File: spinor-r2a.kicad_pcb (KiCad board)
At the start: 2 copper layers, 135 parts, among them Q1 NMOS, Q2 NMOS, Q3 NMOS, Q4 NMOS, Q5 NMOS, Q6 NMOS, U1 TCAN334G, U2 STM32G474CETx, U3 AS5047D, U4 DRV8353FSRTAR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

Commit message: start layout
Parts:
- removed C37: 100uF/63V, hn_lib:hn_C_Kemet_A768MS
- J1, J2, U3: moved to B.Cu
- J9: footprint hn_lib:hn_AMASS_XT30PW-F -> hn_lib:hn_AMASS_XT30PW-M
- L1: value 47uH/400mA -> FB/120R@100MHz; footprint hn_lib:hn_L_Bourns_SRN4026 -> hn_lib:hn_R_0805
- L3: value FB/120R@100MHz -> 47uH/400mA; footprint hn_lib:hn_R_0805 -> hn_lib:hn_L_Bourns_SRN4026
- moved H1 99.5 mm to (191.0, 58.5)
- moved L3 98.1 mm to (64.9, 28.6)
- moved L2 91.4 mm to (64.0, 58.0)
- moved H3 89.4 mm to (191.0, 100.5)
- moved D6 86.1 mm to (210.9, 63.8)
- moved C24 86.1 mm to (215.5, 59.3)
- moved C25 86.1 mm to (215.5, 62.7)
- moved C26 86.1 mm to (202.0, 68.5)
- moved C27 86.1 mm to (217.0, 66.0)
- moved D4 86.1 mm to (210.9, 58.9)
- moved D5 86.1 mm to (210.9, 61.3)
- moved R21 86.1 mm to (205.5, 68.2)
- moved R22 86.1 mm to (205.5, 70.2)
- moved C30 83.7 mm to (202.5, 93.8)
- moved R24 83.7 mm to (206.0, 93.5)
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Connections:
- net Net-(D10-A) renamed /FET_Half_Bridge_C/GATE_H_RAW
- net Net-(D11-A) renamed /FET_Half_Bridge_C/GATE_L_RAW
- net Net-(D4-A) renamed /FET_Half_Bridge_A/GATE_H_RAW
- net Net-(D5-A) renamed /FET_Half_Bridge_A/GATE_L_RAW
- net Net-(D7-A) renamed /FET_Half_Bridge_B/GATE_H_RAW
- net Net-(D8-A) renamed /FET_Half_Bridge_B/GATE_L_RAW
- L1 pad 1: /Power_Supply/3V3_BUCK_SW -> VDD
- L1 pad 2: VDD -> VDDA
- L2 pad 1: VDD -> VBUS
- L2 pad 2: VDDA -> Net-(U5-EN)
- L3 pad 1: VBUS -> /Power_Supply/3V3_BUCK_SW
- L3 pad 2: Net-(U5-EN) -> VDD
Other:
- board outline added: 50 x 63.5 mm

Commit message: placed more components
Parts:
- removed the C30 at (202.5, 93.8)
- removed the C31 at (205.7, 89.0)
- added C36: 4.7uF/50V, hn_lib:hn_C_1206, F.Cu at (81.2, 97.2)
- added C37: 100nF/50V, hn_lib:hn_C_0603, F.Cu at (74.2, 107.6)
- added C38: 4.7uF/50V, hn_lib:hn_C_1206, F.Cu at (132.8, 105.5)
- added C47: 4.7uF/50V, hn_lib:hn_C_1206, F.Cu at (127.8, 105.5)
- added C48: 4.7uF/50V, hn_lib:hn_C_1206, F.Cu at (125.2, 105.5)
- added C49: 4.7uF/50V, hn_lib:hn_C_1206, F.Cu at (126.2, 112.0)
- added C50: 1uF/6.3V, hn_lib:hn_C_0402, F.Cu at (89.3, 101.1)
- added C51: 1uF/6.3V, hn_lib:hn_C_0402, F.Cu at (89.3, 103.0)
- added C52: 4.7uF/50V, hn_lib:hn_C_1206, F.Cu at (169.5, 108.8)
- added C53: 4.7uF/50V, hn_lib:hn_C_1206, F.Cu at (169.5, 113.8)
- added C54: 4.7uF/50V, hn_lib:hn_C_1206, F.Cu at (127.8, 100.5)
- added C55: 4.7uF/50V, hn_lib:hn_C_1206, F.Cu at (125.2, 100.5)
- C24, C28, C33: value 4.7uF/50V -> 100nF/50V; footprint hn_lib:hn_C_1206 -> hn_lib:hn_C_0603
- C25, C29, C32: value 4.7uF/50V -> 2.2nF/6.3V; footprint hn_lib:hn_C_1206 -> hn_lib:hn_C_0402
- C34: value 100nF/50V -> 10uF/6.3V; footprint hn_lib:hn_C_0603 -> hn_lib:hn_C_0805
- C35: value 2.2nF/6.3V -> 100nF/50V; footprint hn_lib:hn_C_0402 -> hn_lib:hn_C_0603
- C39: value 2.2nF/6.3V -> 4.7uF/50V; footprint hn_lib:hn_C_0402 -> hn_lib:hn_C_1206
- C40, C42, C44: value 100nF/50V -> 4.7uF/50V; footprint hn_lib:hn_C_0603 -> hn_lib:hn_C_1206
- C41: value 10uF/6.3V -> 4.7uF/50V; footprint hn_lib:hn_C_0805 -> hn_lib:hn_C_1206
- C45, C46: value 1uF/6.3V -> 4.7uF/50V; footprint hn_lib:hn_C_0402 -> hn_lib:hn_C_1206
- D1, D2, D3: moved to B.Cu
- moved C35 158.4 mm to (74.2, 105.1)
- moved C33 157.0 mm to (74.2, 102.6)
- moved C32 151.4 mm to (79.8, 99.8)
- moved C34 139.2 mm to (78.5, 107.4)
- moved C41 113.1 mm to (157.0, 105.2), turned to 90 degrees
- moved C40 110.4 mm to (159.5, 105.2), turned to 90 degrees
- moved C39 107.2 mm to (153.0, 105.2), turned to 90 degrees
- moved D1 105.5 mm to (148.5, 129.0), turned to -90 degrees
- moved C43 102.0 mm to (126.2, 114.5), turned to 180 degrees
- moved C42 101.3 mm to (150.5, 105.2), turned to 90 degrees
- moved Y1 95.4 mm to (164.5, 85.2), turned to 180 degrees
- moved D2 95.1 mm to (147.6, 136.0), turned to -90 degrees
- moved U1 94.4 mm to (170.2, 95.2), turned to -90 degrees
- moved D3 93.4 mm to (149.4, 136.0), turned to -90 degrees
- moved C24 91.6 mm to (136.8, 106.0), turned to -90 degrees
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- renumbered C36 to C30, C38 to C31
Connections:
- C16 pad 1: GND -> GNDPWR
- C17 pad 1: GND -> GNDPWR
- C17 pad 2: GND -> GNDPWR
- C19 pad 2: GND -> GNDPWR
- C24 pad 2: GND -> /FET_Half_Bridge_A/SHUNT_P
- C25 pad 1: VBUS -> /FET_Half_Bridge_A/SHUNT_P
- C25 pad 2: GND -> GNDPWR
- C26 pad 2: /FET_Half_Bridge_A/SHUNT_P -> /FET_Half_Bridge_B/SHUNT_P
- C27 pad 1: /FET_Half_Bridge_A/SHUNT_P -> /FET_Half_Bridge_B/SHUNT_P
- C27 pad 2: GND -> GNDPWR
- C28 pad 2: GND -> /FET_Half_Bridge_C/SHUNT_P
- C29 pad 1: VBUS -> /FET_Half_Bridge_C/SHUNT_P
- C29 pad 2: GND -> GNDPWR
- C30 pad 2: GND -> GNDPWR
- C31 pad 2: GND -> GNDPWR
- C32 pad 1: VBUS -> /Microcontroller/ADC1_IN3
- C33 pad 1: VBUS -> /Power_Supply/3V3_BUCK_SW
- C33 pad 2: GND -> Net-(U5-CB)
- C34 pad 1: VBUS -> VDD
- C34 pad 2: /FET_Half_Bridge_C/SHUNT_P -> GND
- C35 pad 1: /FET_Half_Bridge_C/SHUNT_P -> VBUS
- C39 pad 1: /Microcontroller/ADC1_IN3 -> VBUS
- C39 pad 2: GND -> GNDPWR
- C40 pad 1: /Power_Supply/3V3_BUCK_SW -> VBUS
- C40 pad 2: Net-(U5-CB) -> GNDPWR
- C41 pad 1: VDD -> VBUS
- C41 pad 2: GND -> GNDPWR
- C42 pad 2: GND -> GNDPWR
- C43 pad 1: Net-(U5-EN) -> VBUS
- C43 pad 2: GND -> GNDPWR
- C44 pad 1: Net-(U5-EN) -> VBUS
- C44 pad 2: GND -> GNDPWR
- C45 pad 1: /Microcontroller/ADC12_IN1 -> VBUS
- C45 pad 2: GND -> GNDPWR
- C46 pad 1: /Microcontroller/ADC12_IN2 -> VBUS
- C46 pad 2: GND -> GNDPWR
- D12 pad 2: GND -> GNDPWR
- D13 pad 2: GND -> GNDPWR
- D6 pad 2: GND -> GNDPWR
- D9 pad 2: GND -> GNDPWR
- J8 pad 1: GND -> GNDPWR
- J9 pad 1: GND -> GNDPWR
- R23 pad 2: GND -> GNDPWR
- R26 pad 2: GND -> GNDPWR
- R29 pad 2: GND -> GNDPWR
- U4 pad 10: GND -> GNDPWR
- U4 pad 11: GND -> GNDPWR
- U4 pad 20: GND -> GNDPWR
- U4 pad 38: GND -> GNDPWR
- U4 pad 39: /Integrated_FET_Driver/GND -> GND
- U4 pad 41: GND -> GNDPWR

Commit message: layout driver and 3v3 buck
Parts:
- removed C35: 100nF/50V, hn_lib:hn_C_0603
- removed L2: FB/120R@100MHz, hn_lib:hn_R_0805
- moved C37 58.0 mm to (129.8, 90.8), turned to -90 degrees
- moved L3 55.9 mm to (129.8, 85.5), turned to 90 degrees
- moved C33 53.7 mm to (125.8, 87.2), turned to 180 degrees
- moved C34 52.9 mm to (126.2, 84.8), turned to -90 degrees
- moved U5 49.5 mm to (126.5, 90.0)
- moved C36 45.4 mm to (126.5, 93.2), turned to 180 degrees
- moved C18 36.3 mm to (139.0, 86.0)
- moved C15 34.0 mm to (137.0, 96.0), turned to 90 degrees
- moved C20 34.0 mm to (134.0, 94.5), turned to -90 degrees
- moved C17 33.3 mm to (133.0, 91.0), turned to 180 degrees
- moved C19 29.9 mm to (135.5, 96.0), turned to -90 degrees
- moved C16 26.8 mm to (132.5, 92.5)
- moved C32 18.1 mm to (97.6, 96.5)
- moved R31 16.3 mm to (97.8, 100.5)
- moved R30 16.3 mm to (97.8, 98.5)
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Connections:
- net Net-(U5-CB) renamed /Power_Supply/3V3_BUCK_CP
- C17 pad 1: GNDPWR -> /Integrated_FET_Driver/DVDD
- C36 pad 1: Net-(U5-EN) -> VBUS
- C37 pad 1: Net-(U5-EN) -> VBUS
- U4 pad 38: GNDPWR -> /Integrated_FET_Driver/DVDD
- U4 pad 39: GND -> GNDPWR
- U5 pad 4: Net-(U5-EN) -> VBUS
- U5 pad 5: Net-(U5-EN) -> VBUS

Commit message: ok
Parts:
- removed C13, C4: 100nF/6.3V, hn_lib:hn_C_0402
- moved C1 96.7 mm to (170.2, 90.8)
- moved R1 93.9 mm to (166.2, 90.8), turned to 180 degrees
- moved R2 93.9 mm to (166.2, 92.6)
- moved C2 89.4 mm to (163.0, 84.8)
- moved C9 81.2 mm to (157.8, 93.5), turned to 180 degrees
- moved R9 79.3 mm to (154.2, 94.8), turned to 90 degrees
- moved R10 77.9 mm to (153.2, 94.8), turned to 90 degrees
- moved C50 77.3 mm to (164.2, 82.0)
- moved R11 76.6 mm to (152.2, 94.8), turned to 90 degrees
- moved J10 76.3 mm to (163.8, 77.8), turned to 180 degrees
- moved C51 75.9 mm to (162.2, 82.0)
- moved R12 75.3 mm to (151.2, 94.8), turned to 90 degrees
- moved C12 75.3 mm to (154.0, 80.2)
- moved C11 74.9 mm to (154.0, 81.2)
- moved R34 73.6 mm to (164.2, 80.0), turned to 180 degrees
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
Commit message: done routing!
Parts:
- removed J3, J4: ~, Connector_PinHeader_1.27mm:PinHeader_1x04_P1.27mm_Vertical
- removed R18: 4.7k, hn_lib:hn_R_0402
- removed R7, R8: 100R, hn_lib:hn_R_0402
- added C4: 100uF/63V, hn_lib:hn_C_Kemet_A768MS, F.Cu at (157.0, 131.0)
- added C58: 4.7uF/50V, hn_lib:hn_C_1206, B.Cu at (160.8, 105.5)
- added C59: 4.7uF/50V, hn_lib:hn_C_1206, B.Cu at (158.2, 105.5)
- added C60: 4.7uF/50V, hn_lib:hn_C_1206, B.Cu at (153.2, 105.5)
- added C61: 4.7uF/50V, hn_lib:hn_C_1206, B.Cu at (145.8, 105.5)
- added C62: 4.7uF/50V, hn_lib:hn_C_1206, B.Cu at (140.8, 105.5)
- added C63: 4.7uF/50V, hn_lib:hn_C_1206, B.Cu at (163.2, 105.5)
- added C64: 4.7uF/50V, hn_lib:hn_C_1206, B.Cu at (148.2, 105.5)
- added C65: 4.7uF/50V, hn_lib:hn_C_1206, B.Cu at (155.8, 105.5)
- added C66: 4.7uF/50V, hn_lib:hn_C_1206, B.Cu at (150.8, 105.5)
- added C67: 4.7uF/50V, hn_lib:hn_C_1206, B.Cu at (143.2, 105.5)
- added C68: 4.7uF/50V, hn_lib:hn_C_1206, B.Cu at (138.2, 105.5)
- added C69: 4.7uF/50V, hn_lib:hn_C_1206, B.Cu at (135.8, 105.5)
- added TP13: ~, Connector_PinHeader_1.00mm:PinHeader_1x01_P1.00mm_Vertical, F.Cu at (162.7, 92.3)
- D1: moved to F.Cu
- D13: moved to B.Cu
- J9: value ~ -> Conn_01x05; footprint hn_lib:hn_AMASS_XT30PW-M -> Connector_PinHeader_2.54mm:PinHeader_1x05_P2.54mm_Vertical
- moved J9 51.2 mm to (132.9, 76.2), turned to 90 degrees
- moved R14 22.5 mm to (170.9, 83.5), turned to 0 degrees
- moved R15 22.5 mm to (170.9, 84.5), turned to 0 degrees
- moved D13 15.7 mm to (132.8, 125.6)
- moved C3 5.59 mm to (148.5, 101.0), turned to 0 degrees
- moved R6 5.43 mm to (138.0, 79.4), turned to 90 degrees
- moved R3 4.94 mm to (141.0, 79.4), turned to 90 degrees
- moved R5 4.88 mm to (139.0, 79.4), turned to 90 degrees
- moved R4 4.70 mm to (140.0, 79.4), turned to 90 degrees
- moved R30 4.16 mm to (164.0, 80.5)
- moved R31 4.16 mm to (164.0, 81.5)
- moved C37 3.93 mm to (126.4, 92.8), turned to 180 degrees
- moved R1 3.34 mm to (165.2, 94.0)
- moved R10 3.26 mm to (156.5, 94.5)
- moved R11 3.26 mm to (155.5, 94.5)
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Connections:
- net /Microcontroller/CANH renamed /Microcontroller/CAN_P
- net /Microcontroller/CANL renamed /Microcontroller/CAN_N
- C16 pad 1: GNDPWR -> GND
- C17 pad 2: GNDPWR -> GND
- C18 pad 1: VDDA -> VDD
- C19 pad 2: GNDPWR -> GND
- C25 pad 2: GNDPWR -> GND
- C27 pad 2: GNDPWR -> GND
- C29 pad 2: GNDPWR -> GND
- C30 pad 2: GNDPWR -> GND
- C31 pad 2: GNDPWR -> GND
- C38 pad 2: GNDPWR -> GND
- C39 pad 2: GNDPWR -> GND
- C40 pad 2: GNDPWR -> GND
- C41 pad 2: GNDPWR -> GND
- C42 pad 2: GNDPWR -> GND
- C43 pad 2: GNDPWR -> GND
- C44 pad 2: GNDPWR -> GND
- C45 pad 2: GNDPWR -> GND
- C46 pad 2: GNDPWR -> GND
- C47 pad 2: GNDPWR -> GND
- C48 pad 2: GNDPWR -> GND
- C49 pad 2: GNDPWR -> GND
- C52 pad 2: GNDPWR -> GND
- C53 pad 2: GNDPWR -> GND
- C54 pad 2: GNDPWR -> GND
- C55 pad 2: GNDPWR -> GND
- D12 pad 2: GNDPWR -> GND
- D13 pad 2: GNDPWR -> GND
- D6 pad 2: GNDPWR -> GND
- D9 pad 2: GNDPWR -> GND
- J8 pad 1: GNDPWR -> GND
- J9 pad 1: GNDPWR -> GND
- J9 pad 2: VBUS -> /Microcontroller/DEBUG_NRST
- R23 pad 2: GNDPWR -> GND
- R26 pad 2: GNDPWR -> GND
- R29 pad 2: GNDPWR -> GND
- R33 pad 1: VDD -> /Microcontroller/ADC12_IN2
- R33 pad 2: /Microcontroller/ADC12_IN2 -> GND
- R35 pad 1: /Microcontroller/ADC12_IN2 -> VDD
- R35 pad 2: GND -> /Microcontroller/ADC12_IN2
- U2 pad 16: /Microcontroller/ADC3_IN12 -> /Microcontroller/ADC1_IN12
- U2 pad 17: /Microcontroller/ADC1_IN12 -> /Microcontroller/ADC2_IN12
- U2 pad 18: /Microcontroller/ADC2_IN12 -> /Microcontroller/ADC3_IN12
- U2 pad 44: /Microcontroller/USART1_RX -> unconnected-(U2-PB7-Pad44)
- U4 pad 10: GNDPWR -> GND
- U4 pad 11: GNDPWR -> GND
- U4 pad 20: GNDPWR -> GND
- U4 pad 25: VDDA -> VDD
- U4 pad 39: GNDPWR -> GND
- U4 pad 41: GNDPWR -> GND
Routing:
- net GND: track 0.00 -> 181.9 mm, vias 0 -> 407
- net VDD: track 0.00 -> 107.2 mm, vias 0 -> 23
- net /Microcontroller/ADC12_IN2: track 0.00 -> 91.4 mm, vias 0 -> 5
- net /Microcontroller/CAN_P: track 0.00 -> 83.4 mm, vias 0 -> 2
- net /Microcontroller/CAN_N: track 0.00 -> 82.1 mm, vias 0 -> 2
- net /Microcontroller/LED_R_K: track 0.00 -> 71.6 mm, vias 0 -> 3
- net /Microcontroller/LED_B_K: track 0.00 -> 69.6 mm, vias 0 -> 3
- net VBUS: track 0.00 -> 48.2 mm, vias 0 -> 127
- net /FET_Half_Bridge_C/PHASE: track 0.00 -> 44.3 mm
- net /Microcontroller/PA11: track 0.00 -> 43.2 mm, vias 0 -> 4
- net /FET_Half_Bridge_C/SHUNT_P: track 0.00 -> 41.9 mm, vias 0 -> 2
- net /Microcontroller/PA7: track 0.00 -> 37.4 mm, vias 0 -> 6
- net /FET_Half_Bridge_C/GATE_L: track 0.00 -> 33.2 mm
- net /Integrated_FET_Driver/SOA: track 0.00 -> 32.1 mm
- net /Microcontroller/NRST: track 0.00 -> 31.1 mm, vias 0 -> 2
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- added copper zone on F.Cu, net /FET_Half_Bridge_A/PHASE
- added copper zone on F.Cu, net /FET_Half_Bridge_A/SHUNT_P
- added copper zone on F.Cu, net /FET_Half_Bridge_B/PHASE
- added copper zone on F.Cu, net /FET_Half_Bridge_B/SHUNT_P
- added copper zone on F.Cu, net /FET_Half_Bridge_C/PHASE
- added copper zone on F.Cu, net /FET_Half_Bridge_C/SHUNT_P
- added copper zone on B.Cu, net GND
- added copper zone on F.Cu, net GND
- added copper zone on In1.Cu, net GND
- added copper zone on B.Cu, net VBUS
- added copper zone on F.Cu, net VBUS
- added copper zone on In2.Cu, net VBUS
- added copper zone on F.Cu, net VDD
- added copper zone on In2.Cu, net VDD
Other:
- copper layers 2 -> 4

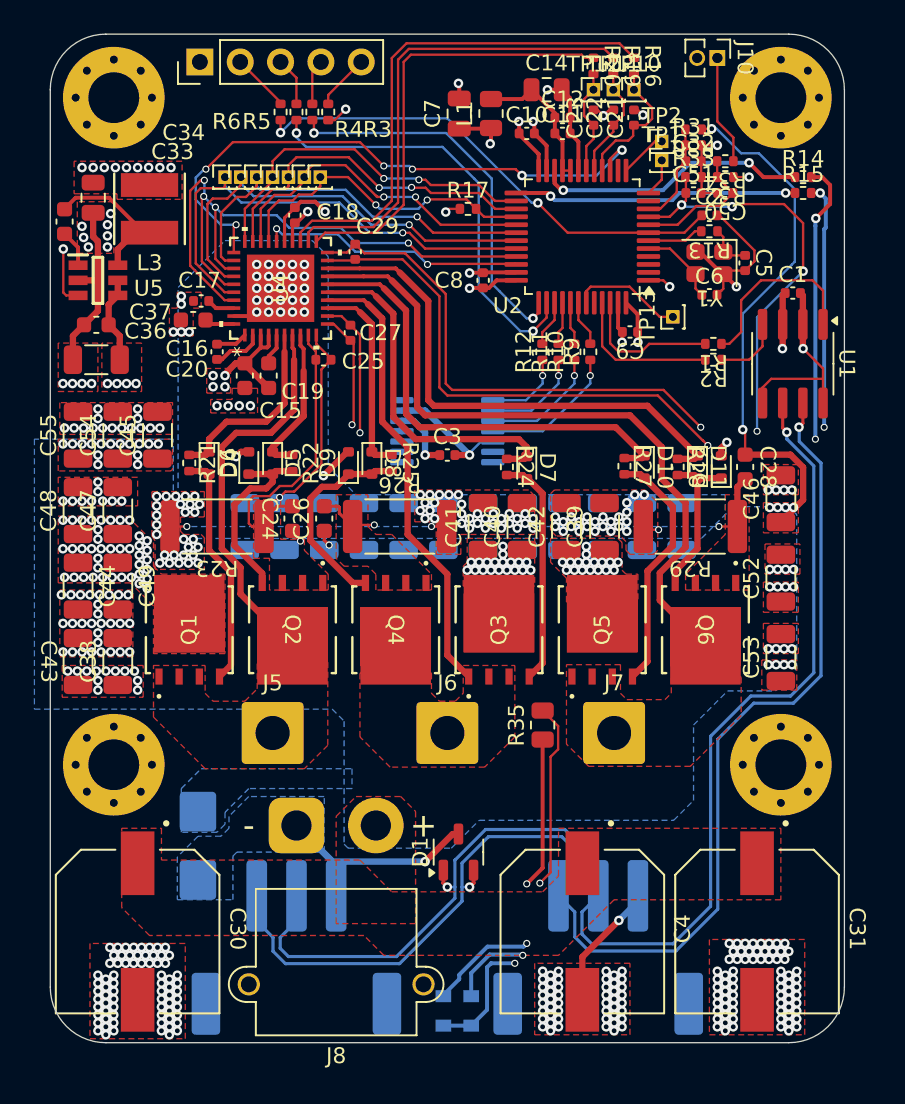
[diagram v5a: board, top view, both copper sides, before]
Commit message: sent to R2.0 to jlcpcb
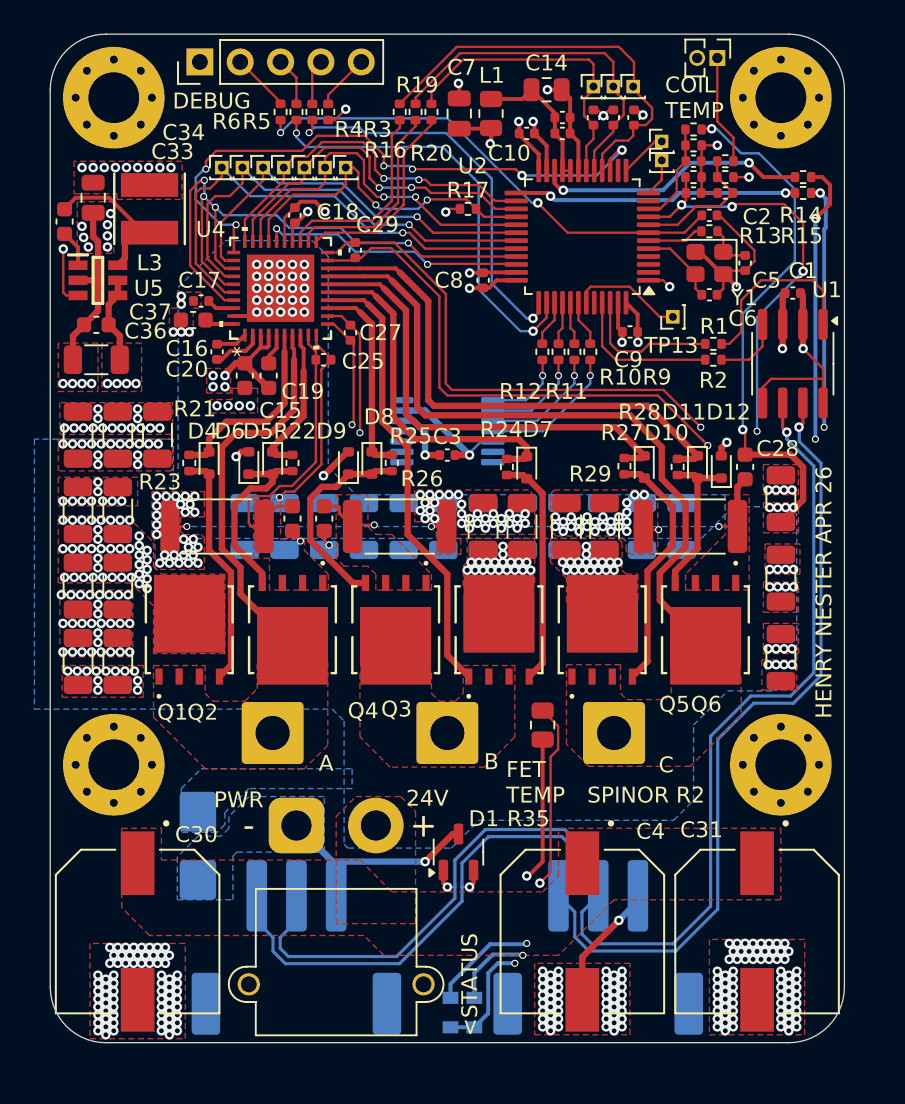
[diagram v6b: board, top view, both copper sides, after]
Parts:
- added G***: LOGO, LOGO, B.Cu at (126.6, 126.5)
- moved R16 15.0 mm to (145.5, 79.4), turned to 90 degrees
- moved R19 12.8 mm to (146.5, 79.4), turned to 90 degrees
- moved R20 10.6 mm to (147.5, 79.4), turned to 90 degrees
- moved TP9 1.71 mm to (142.1, 82.9)
- moved TP8 1.43 mm to (140.8, 82.9)
- moved TP7 1.17 mm to (139.5, 82.9)
- moved TP6 0.92 mm to (138.2, 82.9)
- moved TP3 0.72 mm to (136.9, 82.9)
- moved TP5 0.63 mm to (134.3, 82.9)
- moved TP4 0.61 mm to (135.6, 82.9)
- moved D2 0.46 mm to (148.7, 136.1)
- moved D3 0.22 mm to (150.2, 136.1)
- moved TP10 0.21 mm to (160.2, 77.8)
- moved TP11 0.20 mm to (158.9, 77.8)
- moved TP12 0.20 mm to (157.7, 77.8)
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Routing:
- net /Integrated_FET_Driver/SOA: track 32.1 -> 12.4 mm
- net /Integrated_FET_Driver/SOB: track 30.1 -> 12.6 mm
- net /Microcontroller/ADC1_IN12: track 8.75 -> 26.1 mm
- net /Integrated_FET_Driver/SOC: track 27.7 -> 12.5 mm
- net /Microcontroller/ADC2_IN12: track 7.11 -> 22.1 mm
- net /Microcontroller/ADC3_IN12: track 6.75 -> 19.3 mm
- net /Microcontroller/SPI1_MOSI: track 21.3 -> 22.9 mm
- net /Microcontroller/SPI1_MISO: track 20.3 -> 21.3 mm
- net /Microcontroller/PA7: track 37.4 -> 38.4 mm
- net /Microcontroller/SWDIO: track 24.5 -> 25.1 mm
- net /FET_Half_Bridge_C/SHUNT_P: track 41.9 -> 42.5 mm
- net /Microcontroller/TIM1_CH2: track 27.9 -> 28.4 mm
- net /Microcontroller/SPI1_SCK: track 22.1 -> 22.7 mm
- net GND: vias 407 -> 404
- net VBUS: vias 127 -> 126
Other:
- board text added: "+"
- board text added: "-"
- board text added: "2 1 DAC"
- board text added: "24V"
- board text added: "<STATUS"
- board text added: "A"
- board text added: "B"
- board text added: "C"
- board text added: "CAN"
- board text added: "CLK"
- board text added: "COIL TEMP"
- board text added: "CONTROLLER FOR"
- board text added: "CORTEX M4+FPU"
- board text added: "DEBUG"
- board text added: "DIO"
- board text added: "E"
- board text added: "FET TEMP"
- board text added: "FIELD-ORIENTED"
- board text added: "G"
- board text added: "GND"
- board text added: "H"
- board text added: "HENRY NESTER APR 26"
- board text added: "IABC"
- board text added: "L"
- board text added: "PWR"
- board text added: "R2"
- board text added: "ROBOTICS"
- board text added: "ROTOR"
- board text added: "RST"
- board text added: "SPINOR"
- board text added: "SPINOR R2"
- board text added: "STATOR"
- board text added: "TX"
- board text added: "VTG"
- board text added: "d"
- board text added: "q"
- board text added: "θ"
- board text added: "φ"
- board text added: "∠(B) ENCODER"
